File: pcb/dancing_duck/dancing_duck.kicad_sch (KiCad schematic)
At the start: 11 parts, among them J1 Conn_01x02, J2 Conn_01x02, J3 Conn_01x02, J4 Conn_01x02, J5 Conn_01x02_Pin, J6 Conn_01x01_Pin

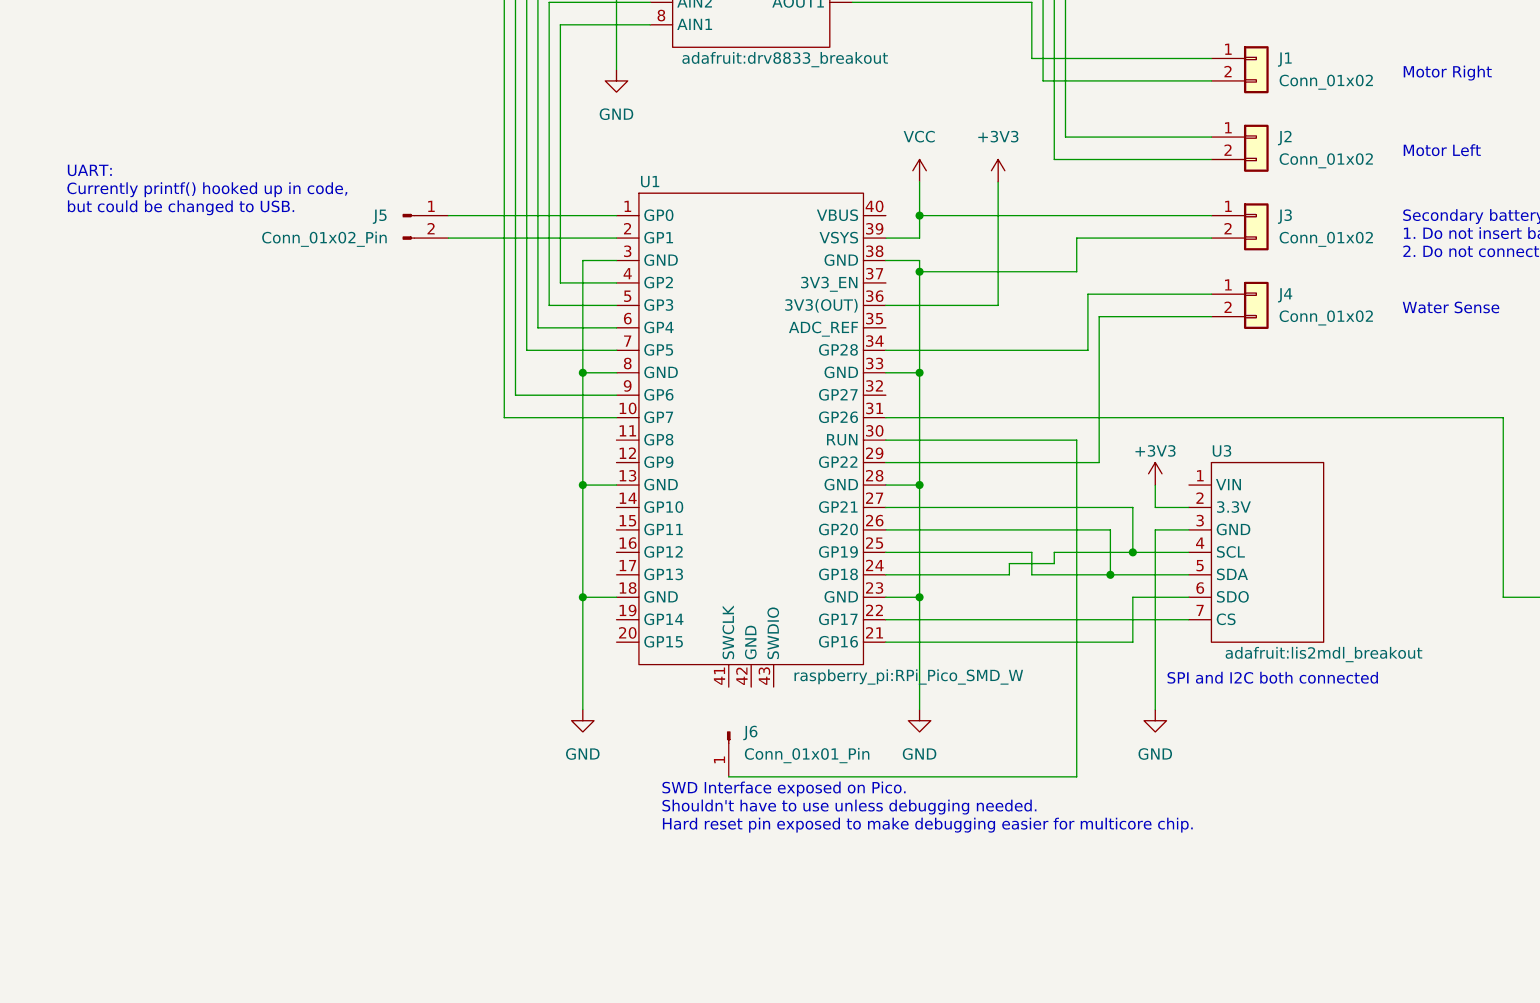
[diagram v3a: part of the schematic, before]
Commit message: fix: update pcb to beta
- Fix daughter board pin hole size
- Add better support for connecting J-Link
- Update silkscreen
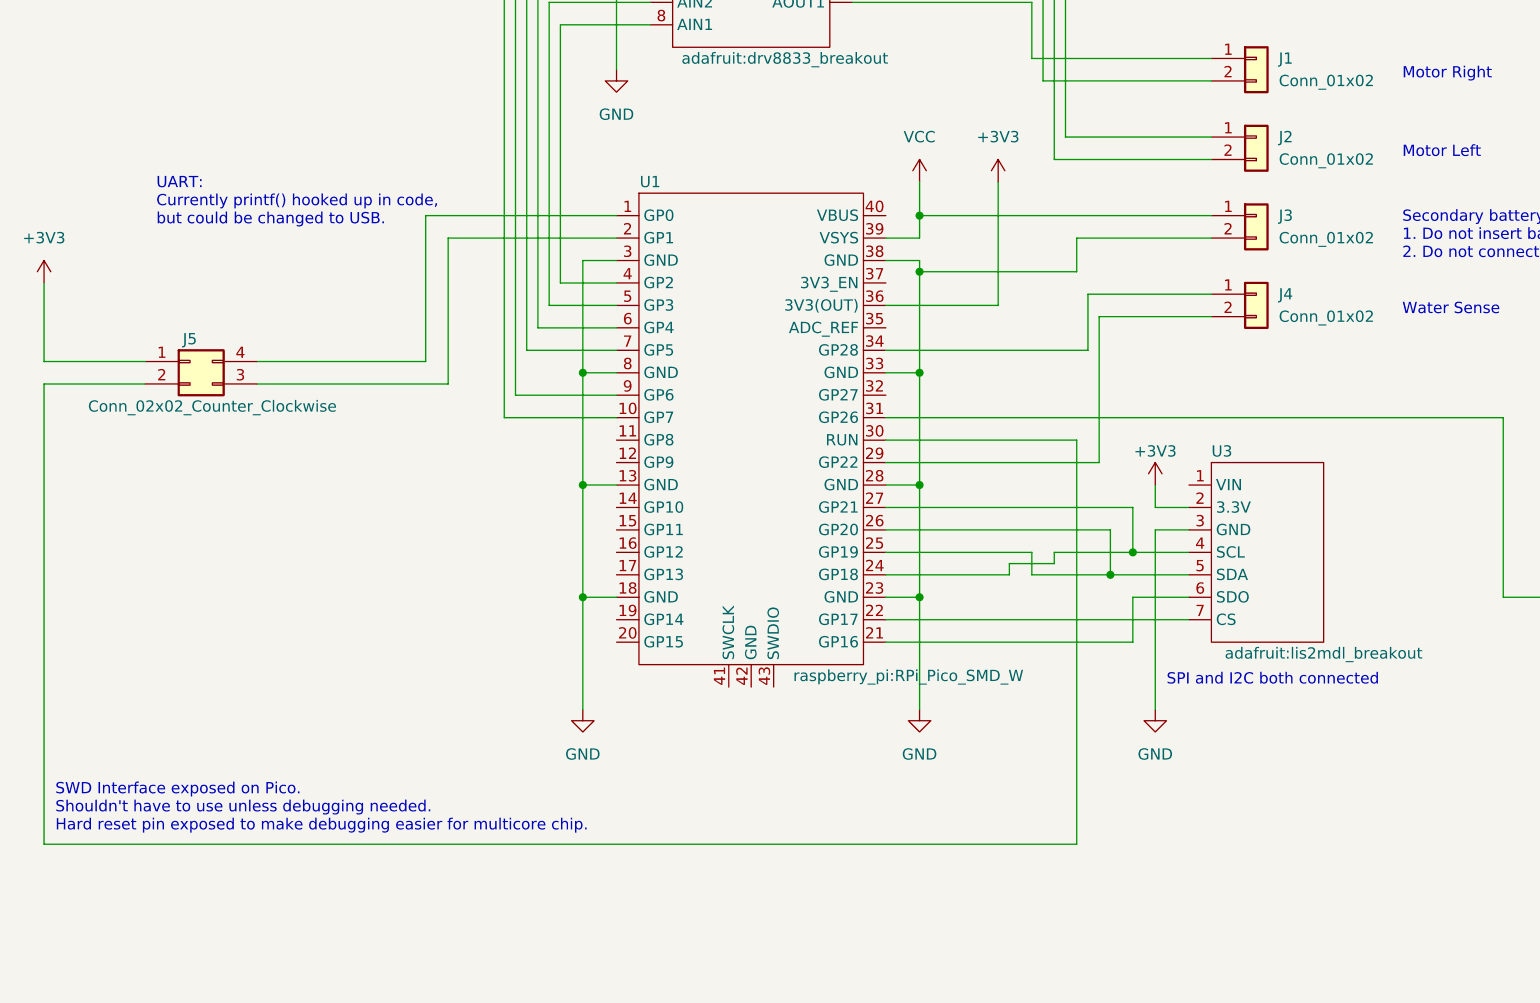
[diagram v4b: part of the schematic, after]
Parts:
- removed J5: Conn_01x02_Pin, Connector_PinHeader_2.54mm:PinHeader_1x02_P2.54mm_Vertical, symbol Connector:Conn_01x02_Pin
- removed J6: Conn_01x01_Pin, Connector_PinHeader_2.54mm:PinHeader_1x01_P2.54mm_Vertical, symbol Connector:Conn_01x01_Pin
- added J5: Conn_02x02_Counter_Clockwise, Connector_PinHeader_2.54mm:PinHeader_2x02_P2.54mm_Vertical, symbol Connector_Generic:Conn_02x02_Counter_Clockwise
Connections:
- net +3V3: now also J5.1 (Pin_1)
- net at U1.1 (GP0): now also J5.4 (Pin_4)
- net at U1.2 (GP1): now also J5.3 (Pin_3)
- net at U1.30 (RUN): now also J5.2 (Pin_2)
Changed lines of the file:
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@@
   (title_block
     (title "Dancing Duck Carrier Board")
-    (date "2024-06-30")
-    (rev "Alpha")
+    (date "2024-07-12")
+    (rev "Beta")
     (company "Shadow Grove Lab/Seattle Design Nerds")
+    (comment 1 "Designer: Josh Erickson")
   )
   (junction (at 78.74 121.92) (diameter 0) (color 0 0 0 0)
@@
     (stroke (width 0) (type default))
   )
-  (wire (pts (xy 134.62 154.94) (xy 134.62 116.84))
+  (wire (pts (xy 134.62 162.56) (xy 134.62 116.84))
     (stroke (width 0) (type default))
   )
@@
     (stroke (width 0) (type default))
   )
-  (wire (pts (xy 63.5 91.44) (xy 82.55 91.44))
+  (wire (pts (xy 60.96 91.44) (xy 82.55 91.44))
     (stroke (width 0) (type default))
   )
@@
     (stroke (width 0) (type default))
   )
+  (wire (pts (xy 41.91 110.49) (xy 63.5 110.49))
+    (stroke (width 0) (type default))
+  )
   (wire (pts (xy 82.55 99.06) (xy 76.2 99.06))
     (stroke (width 0) (type default))
   )
+  (wire (pts (xy 17.78 107.95) (xy 17.78 99.06))
+    (stroke (width 0) (type default))
+  )
   (wire (pts (xy 72.39 62.23) (xy 86.36 62.23))
     (stroke (width 0) (type default))
@@
     (stroke (width 0) (type default))
   )
+  (wire (pts (xy 41.91 107.95) (xy 60.96 107.95))
+    (stroke (width 0) (type default))
+  )
   (wire (pts (xy 138.43 127) (xy 138.43 132.08))
     (stroke (width 0) (type default))
@@
     (stroke (width 0) (type default))
   )
+  (wire (pts (xy 17.78 107.95) (xy 29.21 107.95))
+    (stroke (width 0) (type default))
+  )
   (wire (pts (xy 143.51 124.46) (xy 143.51 121.92))
     (stroke (width 0) (type default))
@@
     (stroke (width 0) (type default))
   )
+  (wire (pts (xy 60.96 107.95) (xy 60.96 91.44))
+    (stroke (width 0) (type default))
+  )
   (wire (pts (xy 135.89 106.68) (xy 135.89 100.33))
     (stroke (width 0) (type default))
@@
     (stroke (width 0) (type default))
   )
+  (wire (pts (xy 63.5 93.98) (xy 63.5 110.49))
+    (stroke (width 0) (type default))
+  )
   (wire (pts (xy 82.55 134.62) (xy 78.74 134.62))
     (stroke (width 0) (type default))
   )
+  (wire (pts (xy 17.78 162.56) (xy 17.78 110.49))
+    (stroke (width 0) (type default))
+  )
   (wire (pts (xy 116.84 93.98) (xy 116.84 91.44))
     (stroke (width 0) (type default))
@@
     (stroke (width 0) (type default))
   )
-  (wire (pts (xy 95.25 154.94) (xy 134.62 154.94))
+  (wire (pts (xy 17.78 162.56) (xy 134.62 162.56))
     (stroke (width 0) (type default))
   )
@@
   )
   (wire (pts (xy 74.93 67.31) (xy 86.36 67.31))
+    (stroke (width 0) (type default))
+  )
+  (wire (pts (xy 17.78 110.49) (xy 29.21 110.49))
     (stroke (width 0) (type default))
   )
@@
   )
   (text "UART:\nCurrently printf() hooked up in code, \nbut could be changed to USB."
-    (at 20.32 91.44 0)
+    (at 30.48 92.71 0)
     (effects (font (size 1.27 1.27)) (justify left bottom))
   )
@@
   )
   (text "SWD Interface exposed on Pico.\nShouldn't have to use unless debugging needed.\nHard reset pin exposed to make debugging easier for multicore chip."
-    (at 87.63 161.29 0)
+    (at 19.05 161.29 0)
     (effects (font (size 1.27 1.27)) (justify left bottom))
   )
@@
         (path "/adb842c0-33ba-4e81-bd0d-80db0bf23605"
           (reference "#PWR04") (unit 1)
+        )
+      )
+    )
+  )
+  (symbol (lib_id "power:+3V3") (at 17.78 99.06 0) (unit 1)
+    (in_bom yes) (on_board yes) (dnp no) (fields_autoplaced)
+    (property "Reference" "#PWR011" (at 17.78 102.87 0)
+      (effects (font (size 1.27 1.27)) hide)
+    )
+    (property "Value" "+3V3" (at 17.78 93.98 0)
+      (effects (font (size 1.27 1.27)))
+    )
+    (property "Footprint" "" (at 17.78 99.06 0)
+      (effects (font (size 1.27 1.27)) hide)
+    )
+    (property "Datasheet" "" (at 17.78 99.06 0)
+      (effects (font (size 1.27 1.27)) hide)
+    )
+    (pin "1")
+    (instances
+      (project "dancing_duck"
+        (path "/adb842c0-33ba-4e81-bd0d-80db0bf23605"
+          (reference "#PWR011") (unit 1)
         )
       )
@@
     )
   )
-  (symbol (lib_id "Connector:Conn_01x02_Pin") (at 58.42 91.44 0) (unit 1)
+  (symbol (lib_id "Device:R_US") (at 190.5 129.54 0) (unit 1)
+    (in_bom yes) (on_board yes) (dnp no) (fields_autoplaced)
+    (property "Reference" "R1" (at 193.04 128.27 0)
+      (effects (font (size 1.27 1.27)) (justify left))
+    )
+    (property "Value" "220k" (at 193.04 130.81 0)
+      (effects (font (size 1.27 1.27)) (justify left))
+    )
+    (property "Footprint" "Resistor_SMD:R_1206_3216Metric_Pad1.30x1.75mm_HandSolder" (at 191.516 129.794 90)
+      (effects (font (size 1.27 1.27)) hide)
+    )
+    (property "Datasheet" "~" (at 190.5 129.54 0)
+      (effects (font (size 1.27 1.27)) hide)
+    )
+    (pin "2")
+    (pin "1")
+    (instances
+      (project "dancing_duck"
+        (path "/adb842c0-33ba-4e81-bd0d-80db0bf23605"
+          (reference "R1") (unit 1)
+        )
+      )
+    )
+  )
+  (symbol (lib_id "Connector_Generic:Conn_02x02_Counter_Clockwise") (at 34.29 107.95 0) (unit 1)
     (in_bom yes) (on_board yes) (dnp no)
-    (property "Reference" "J5" (at 55.88 91.44 0)
-      (effects (font (size 1.27 1.27)))
-    )
-    (property "Value" "Conn_01x02_Pin" (at 49.53 93.98 0)
-      (effects (font (size 1.27 1.27)))
-    )
-    (property "Footprint" "Connector_PinHeader_2.54mm:PinHeader_1x02_P2.54mm_Vertical" (at 58.42 91.44 0)
-      (effects (font (size 1.27 1.27)) hide)
-    )
-    (property "Datasheet" "~" (at 58.42 91.44 0)
-      (effects (font (size 1.27 1.27)) hide)
-    )
-    (pin "1")
+    (property "Reference" "J5" (at 34.29 105.41 0)
+      (effects (font (size 1.27 1.27)))
+    )
+    (property "Value" "Conn_02x02_Counter_Clockwise" (at 36.83 113.03 0)
+      (effects (font (size 1.27 1.27)))
+    )
+    (property "Footprint" "Connector_PinHeader_2.54mm:PinHeader_2x02_P2.54mm_Vertical" (at 34.29 107.95 0)
+      (effects (font (size 1.27 1.27)) hide)
+    )
+    (property "Datasheet" "~" (at 34.29 107.95 0)
+      (effects (font (size 1.27 1.27)) hide)
+    )
     (pin "2")
+    (pin "4")
+    (pin "1")
+    (pin "3")
     (instances
       (project "dancing_duck"
@@
         )
       )
-    )
-  )
-  (symbol (lib_id "Device:R_US") (at 190.5 129.54 0) (unit 1)
-    (in_bom yes) (on_board yes) (dnp no) (fields_autoplaced)
-    (property "Reference" "R1" (at 193.04 128.27 0)
-      (effects (font (size 1.27 1.27)) (justify left))
-    )
-    (property "Value" "220k" (at 193.04 130.81 0)
-      (effects (font (size 1.27 1.27)) (justify left))
-    )
-    (property "Footprint" "Resistor_SMD:R_1206_3216Metric_Pad1.30x1.75mm_HandSolder" (at 191.516 129.794 90)
-      (effects (font (size 1.27 1.27)) hide)
-    )
-    (property "Datasheet" "~" (at 190.5 129.54 0)
-      (effects (font (size 1.27 1.27)) hide)
-    )
-    (pin "2")
-    (pin "1")
-    (instances
-      (project "dancing_duck"
-        (path "/adb842c0-33ba-4e81-bd0d-80db0bf23605"
-          (reference "R1") (unit 1)
-        )
-      )
-    )
-  )
-  (symbol (lib_id "Connector:Conn_01x01_Pin") (at 95.25 149.86 270) (unit 1)
-    (in_bom yes) (on_board yes) (dnp no)
-    (property "Reference" "J6" (at 97.79 149.86 90)
-      (effects (font (size 1.27 1.27)))
-    )
-    (property "Value" "Conn_01x01_Pin" (at 104.14 152.4 90)
-      (effects (font (size 1.27 1.27)))
-    )
-    (property "Footprint" "Connector_PinHeader_2.54mm:PinHeader_1x01_P2.54mm_Vertical" (at 95.25 149.86 0)
-      (effects (font (size 1.27 1.27)) hide)
-    )
-    (property "Datasheet" "~" (at 95.25 149.86 0)
-      (effects (font (size 1.27 1.27)) hide)
-    )
-    (pin "1")
-    (instances
-      (project "dancing_duck"
-        (path "/adb842c0-33ba-4e81-bd0d-80db0bf23605"
-          (reference "J6") (unit 1)
-        )
-      )

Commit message: fix: add capacitor to pcb
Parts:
- added C1: 1000pf, Capacitor_SMD:C_1206_3216Metric_Pad1.33x1.80mm_HandSolder, symbol Device:C
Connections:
- net GND: now also C1.2
- net at R1.2, R2.1, U1.31 (GP26): now also C1.1
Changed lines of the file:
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@@
   (junction (at 116.84 109.22) (diameter 0) (color 0 0 0 0)
   )
+  (junction (at 190.5 144.78) (diameter 0) (color 0 0 0 0)
+  )
   (junction (at 78.74 109.22) (diameter 0) (color 0 0 0 0)
   )
+  (junction (at 177.8 134.62) (diameter 0) (color 0 0 0 0)
+  )
   (junction (at 78.74 134.62) (diameter 0) (color 0 0 0 0)
   )
@@
     (stroke (width 0) (type default))
   )
-  (wire (pts (xy 113.03 114.3) (xy 182.88 114.3))
+  (wire (pts (xy 113.03 114.3) (xy 177.8 114.3))
     (stroke (width 0) (type default))
   )
@@
     (stroke (width 0) (type default))
   )
-  (wire (pts (xy 182.88 134.62) (xy 190.5 134.62))
+  (wire (pts (xy 177.8 134.62) (xy 190.5 134.62))
     (stroke (width 0) (type default))
   )
@@
     (stroke (width 0) (type default))
   )
-  (wire (pts (xy 182.88 114.3) (xy 182.88 134.62))
+  (wire (pts (xy 177.8 114.3) (xy 177.8 134.62))
     (stroke (width 0) (type default))
   )
@@
     (stroke (width 0) (type default))
   )
+  (wire (pts (xy 177.8 134.62) (xy 177.8 135.89))
+    (stroke (width 0) (type default))
+  )
   (wire (pts (xy 190.5 123.19) (xy 190.5 125.73))
     (stroke (width 0) (type default))
@@
     (stroke (width 0) (type default))
   )
+  (wire (pts (xy 177.8 143.51) (xy 177.8 144.78))
+    (stroke (width 0) (type default))
+  )
   (wire (pts (xy 76.2 69.85) (xy 86.36 69.85))
     (stroke (width 0) (type default))
@@
     (stroke (width 0) (type default))
   )
+  (wire (pts (xy 177.8 144.78) (xy 190.5 144.78))
+    (stroke (width 0) (type default))
+  )
   (wire (pts (xy 69.85 114.3) (xy 69.85 57.15))
     (stroke (width 0) (type default))
@@
     (stroke (width 0) (type default))
   )
+  (wire (pts (xy 190.5 144.78) (xy 190.5 146.05))
+    (stroke (width 0) (type default))
+  )
   (wire (pts (xy 109.22 62.23) (xy 132.08 62.23))
     (stroke (width 0) (type default))
@@
     (stroke (width 0) (type default))
   )
-  (wire (pts (xy 190.5 143.51) (xy 190.5 146.05))
+  (wire (pts (xy 190.5 143.51) (xy 190.5 144.78))
     (stroke (width 0) (type default))
   )
@@
         (path "/adb842c0-33ba-4e81-bd0d-80db0bf23605"
           (reference "#PWR01") (unit 1)
+        )
+      )
+    )
+  )
+  (symbol (lib_id "Device:C") (at 177.8 139.7 0) (unit 1)
+    (in_bom yes) (on_board yes) (dnp no) (fields_autoplaced)
+    (property "Reference" "C1" (at 181.61 138.43 0)
+      (effects (font (size 1.27 1.27)) (justify left))
+    )
+    (property "Value" "1000pf" (at 181.61 140.97 0)
+      (effects (font (size 1.27 1.27)) (justify left))
+    )
+    (property "Footprint" "Capacitor_SMD:C_1206_3216Metric_Pad1.33x1.80mm_HandSolder" (at 178.7652 143.51 0)
+      (effects (font (size 1.27 1.27)) hide)
+    )
+    (property "Datasheet" "~" (at 177.8 139.7 0)
+      (effects (font (size 1.27 1.27)) hide)
+    )
+    (property "Part Num" "CL31B102KGFNNNE" (at 177.8 139.7 0)
+      (effects (font (size 1.27 1.27)) hide)
+    )
+    (pin "1")
+    (pin "2")
+    (instances
+      (project "dancing_duck"
+        (path "/adb842c0-33ba-4e81-bd0d-80db0bf23605"
+          (reference "C1") (unit 1)
         )
       )
@@
       (effects (font (size 1.27 1.27)))
     )
-    (property "Footprint" "adafruit:lis2mdl_breakout" (at 162.56 140.97 0)
-      (effects (font (size 1.27 1.27)))
-    )
+    (property "Footprint" "adafruit:lis2mdl_breakout" (at 160.02 140.97 0)
+      (effects (font (size 1.27 1.27)))
+    )

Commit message: feat: add RX to GND solder bridge to PCB
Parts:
- added R3: 0 DNP, Jumper:SolderJumper-2_P1.3mm_Open_TrianglePad1.0x1.5mm, symbol Device:R_US
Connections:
- net GND: now also R3.2
- net at J5.3 (Pin_3), U1.2 (GP1): now also R3.1
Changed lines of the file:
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@@
     (comment 1 "Designer: Josh Erickson")
   )
+  (junction (at 54.61 110.49) (diameter 0) (color 0 0 0 0)
+  )
   (junction (at 78.74 121.92) (diameter 0) (color 0 0 0 0)
   )
@@
     (stroke (width 0) (type default))
   )
-  (wire (pts (xy 41.91 110.49) (xy 63.5 110.49))
+  (wire (pts (xy 41.91 110.49) (xy 54.61 110.49))
     (stroke (width 0) (type default))
   )
@@
     (stroke (width 0) (type default))
   )
+  (wire (pts (xy 54.61 125.73) (xy 54.61 134.62))
+    (stroke (width 0) (type default))
+  )
   (wire (pts (xy 113.03 127) (xy 138.43 127))
     (stroke (width 0) (type default))
@@
     (stroke (width 0) (type default))
   )
+  (wire (pts (xy 54.61 110.49) (xy 54.61 118.11))
+    (stroke (width 0) (type default))
+  )
   (wire (pts (xy 113.03 132.08) (xy 127 132.08))
     (stroke (width 0) (type default))
@@
   )
   (wire (pts (xy 17.78 162.56) (xy 134.62 162.56))
+    (stroke (width 0) (type default))
+  )
+  (wire (pts (xy 54.61 110.49) (xy 63.5 110.49))
     (stroke (width 0) (type default))
   )
@@
         (path "/adb842c0-33ba-4e81-bd0d-80db0bf23605"
           (reference "#PWR010") (unit 1)
+        )
+      )
+    )
+  )
+  (symbol (lib_id "power:GND") (at 54.61 134.62 0) (unit 1)
+    (in_bom yes) (on_board yes) (dnp no) (fields_autoplaced)
+    (property "Reference" "#PWR012" (at 54.61 140.97 0)
+      (effects (font (size 1.27 1.27)) hide)
+    )
+    (property "Value" "GND" (at 54.61 139.7 0)
+      (effects (font (size 1.27 1.27)))
+    )
+    (property "Footprint" "" (at 54.61 134.62 0)
+      (effects (font (size 1.27 1.27)) hide)
+    )
+    (property "Datasheet" "" (at 54.61 134.62 0)
+      (effects (font (size 1.27 1.27)) hide)
+    )
+    (pin "1")
+    (instances
+      (project "dancing_duck"
+        (path "/adb842c0-33ba-4e81-bd0d-80db0bf23605"
+          (reference "#PWR012") (unit 1)
         )
       )
@@
         )
       )
+    )
+  )
+  (symbol (lib_id "Device:R_US") (at 54.61 121.92 0) (unit 1)
+    (in_bom yes) (on_board yes) (dnp no) (fields_autoplaced)
+    (property "Reference" "R3" (at 57.15 120.65 0)
+      (effects (font (size 1.27 1.27)) (justify left))
+    )
+    (property "Value" "0 DNP" (at 57.15 123.19 0)
+      (effects (font (size 1.27 1.27)) (justify left))
+    )
+    (property "Footprint" "Jumper:SolderJumper-2_P1.3mm_Open_TrianglePad1.0x1.5mm" (at 55.626 122.174 90)
+      (effects (font (size 1.27 1.27)) hide)
+    )
+    (property "Datasheet" "~" (at 54.61 121.92 0)
+      (effects (font (size 1.27 1.27)) hide)
+    )
+    (pin "2")
+    (pin "1")
+    (instances
+      (project "dancing_duck"
+        (path "/adb842c0-33ba-4e81-bd0d-80db0bf23605"
+          (reference "R3") (unit 1)
+        )
+      )
